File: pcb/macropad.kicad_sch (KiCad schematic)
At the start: 17 parts, among them J1 OLED_DISPLAY, SW1 SW_Push, SW2 SW_Push, SW3 SW_Push, SW4 SW_Push, SW5 RotaryEncoder_Switch, SW6 SW_Push, U1 Seeed Studio XIAO RP2040

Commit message: V1.2 - Fixed the LED symbols and retraced everything
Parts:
- D7, D8, D9: footprint Hackpad:SK6812MINI-E_fixed -> LED_SMD:LED_SK6812MINI-E_3.2x2.8mm_P1.5mm_ReverseMount; symbol LED:WS2812B -> LED:SK6812MINI-E
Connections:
- net GND: now also D7.1 (VSS), D8.1 (VSS), D9.1 (VSS); no longer D7.3 (VSS), D8.3 (VSS), D9.3 (VSS)
- net VCC: now also D7.3 (VDD), D8.3 (VDD), D9.3 (VDD); no longer D7.1 (VDD), D8.1 (VDD), D9.1 (VDD)
- net at D9.2 (DIN): now also U1.11 (PA6_A10_D10_MOSI); no longer D8.4 (DIN)
- net at D9.4 (DOUT): now also D8.2 (DIN); no longer U1.11 (PA6_A10_D10_MOSI)
- net at D7.2 (DIN): now also D8.4 (DOUT)
- net at D7.4 (DOUT): no longer D8.2 (DOUT)
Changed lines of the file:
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@@
 	)
 	(symbol
-		(lib_id "LED:WS2812B")
+		(lib_id "LED:SK6812MINI-E")
 		(at 228.6 74.93 90)
 		(unit 1)
@@
 			)
 		)
-		(property "Footprint" "Hackpad:SK6812MINI-E_fixed"
+		(property "Footprint" "LED_SMD:LED_SK6812MINI-E_3.2x2.8mm_P1.5mm_ReverseMount"
 			(at 236.22 73.66 0)
 			(hide yes)
@@
 			)
 		)
-		(property "Datasheet" "https://cdn-shop.adafruit.com/datasheets/WS2812B.pdf"
+		(property "Datasheet" "https://www.lcsc.com/datasheet/C5149201.pdf"
 			(at 238.125 72.39 0)
 			(hide yes)
@@
 	)
 	(symbol
-		(lib_id "LED:WS2812B")
+		(lib_id "LED:SK6812MINI-E")
 		(at 228.6 27.94 90)
 		(unit 1)
@@
 			)
 		)
-		(property "Footprint" "Hackpad:SK6812MINI-E_fixed"
+		(property "Footprint" "LED_SMD:LED_SK6812MINI-E_3.2x2.8mm_P1.5mm_ReverseMount"
 			(at 236.22 26.67 0)
 			(hide yes)
@@
 			)
 		)
-		(property "Datasheet" "https://cdn-shop.adafruit.com/datasheets/WS2812B.pdf"
+		(property "Datasheet" "https://www.lcsc.com/datasheet/C5149201.pdf"
 			(at 238.125 25.4 0)
 			(hide yes)
@@
 	)
 	(symbol
-		(lib_id "LED:WS2812B")
+		(lib_id "LED:SK6812MINI-E")
 		(at 228.6 52.07 90)
 		(unit 1)
@@
 			)
 		)
-		(property "Footprint" "Hackpad:SK6812MINI-E_fixed"
+		(property "Footprint" "LED_SMD:LED_SK6812MINI-E_3.2x2.8mm_P1.5mm_ReverseMount"
 			(at 236.22 50.8 0)
 			(hide yes)
@@
 			)
 		)
-		(property "Datasheet" "https://cdn-shop.adafruit.com/datasheets/WS2812B.pdf"
+		(property "Datasheet" "https://www.lcsc.com/datasheet/C5149201.pdf"
 			(at 238.125 49.53 0)
 			(hide yes)

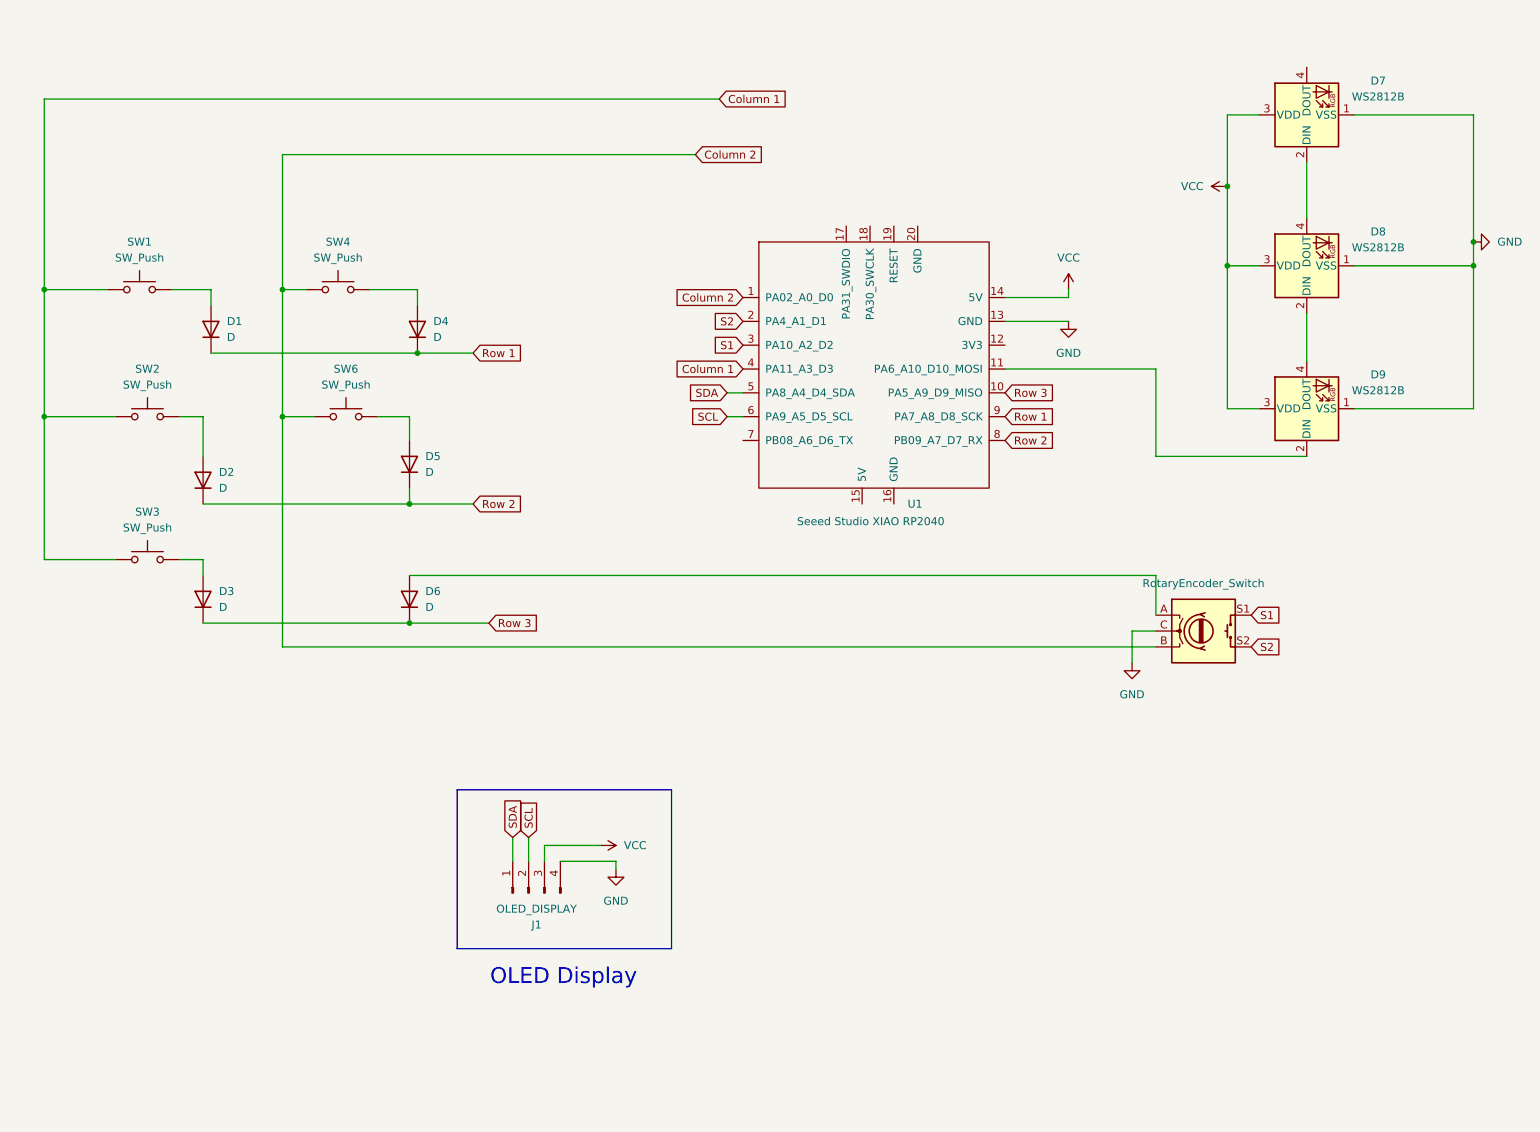
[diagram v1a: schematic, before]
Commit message: V1.3 - Added switch LEDs and GND fields
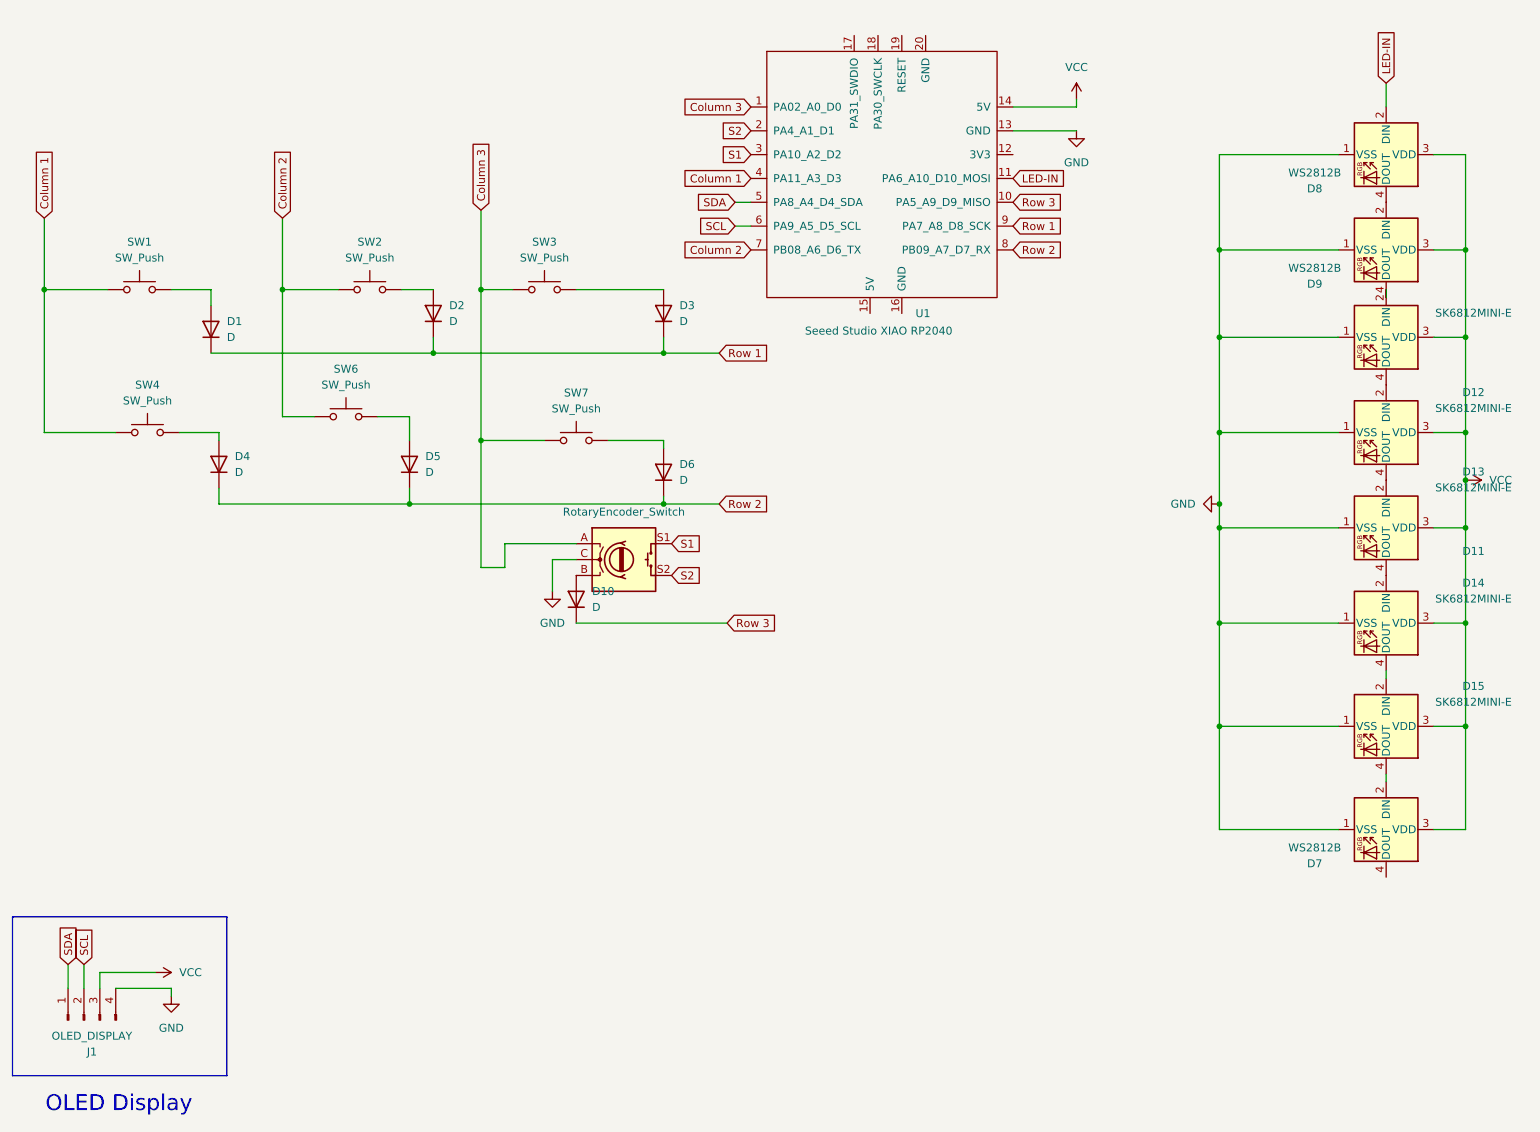
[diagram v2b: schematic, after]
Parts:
- added D10: D, Diode_THT:D_DO-35_SOD27_P7.62mm_Horizontal, symbol Device:D
- added D11, D12, D13, D14, D15: SK6812MINI-E, Cherry-MX:MX_SK6812MINI-E, symbol LED:SK6812MINI-E
- added SW7: SW_Push, Button_Switch_Keyboard:SW_Cherry_MX_1.00u_PCB, symbol Switch:SW_Push
- D9: footprint LED_SMD:LED_SK6812MINI-E_3.2x2.8mm_P1.5mm_ReverseMount -> Cherry-MX:MX_SK6812MINI-E
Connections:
- net Column 1: now also SW4.1; no longer SW2.1, SW3.1
- net Column 2: now also SW2.1, U1.7 (PB08_A6_D6_TX); no longer SW4.1, SW5.B, U1.1 (PA02_A0_D0)
- net GND: now also D11.1 (VSS), D12.1 (VSS), D13.1 (VSS), D14.1 (VSS), D15.1 (VSS)
- net Row 1: now also D2.1 (K), D3.1 (K); no longer D4.1 (K)
- net Row 2: now also D4.1 (K), D6.1 (K); no longer D2.1 (K)
- net Row 3: now also D10.1 (K); no longer D3.1 (K), D6.1 (K)
- net VCC: now also D11.3 (VDD), D12.3 (VDD), D13.3 (VDD), D14.3 (VDD), D15.3 (VDD)
- net at D9.2 (DIN): now also D8.4 (DOUT); no longer U1.11 (PA6_A10_D10_MOSI)
- net at D9.4 (DOUT): now also D11.2 (DIN); no longer D8.2 (DIN)
- net at D6.2 (A): now also SW7.2; no longer SW5.A
- net at D7.2 (DIN): now also D15.4 (DOUT); no longer D8.4 (DOUT)
- new net: D11.4 (DOUT), D12.2 (DIN)
- new net: D13.4 (DOUT), D14.2 (DIN)
- new net: D14.4 (DOUT), D15.2 (DIN)
- new net: D10.2 (A), SW5.B
- new net: D12.4 (DOUT), D13.2 (DIN)
- new net Column 3: SW3.1, SW5.A, SW7.1, U1.1 (PA02_A0_D0)
- new net LED-IN: D8.2 (DIN), U1.11 (PA6_A10_D10_MOSI)
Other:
- moved on the sheet: D2, D3, D4, D6, D7, D8, D9, J1, SW2, SW3, SW4, U1

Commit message: V1.5 - Fixed faulty encoder wiring, retraced
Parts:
- D11, D12, D13, D14, D15, D9: footprint Cherry-MX:MX_SK6812MINI-E -> Libraries:MX_SK6812MINI-E
- D7, D8: footprint LED_SMD:LED_SK6812MINI-E_3.2x2.8mm_P1.5mm_ReverseMount -> Libraries:SK6812MINI-E_fixed
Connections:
- net Column 3: now also SW5.S1; no longer SW5.A
- net at D10.2 (A): now also SW5.S2; no longer SW5.B
- net S1 renamed EN_B
- net EN_B: now also SW5.B; no longer SW5.S1
- net S2 renamed EN_A
- net EN_A: now also SW5.A; no longer SW5.S2
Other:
- moved on the sheet: D10
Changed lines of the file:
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@@
 	(wire
 		(pts
+			(xy 100.33 92.71) (xy 132.08 92.71)
+		)
+		(stroke
+			(width 0)
+			(type default)
+		)
+	)
+	(wire
+		(pts
 			(xy 233.68 125.73) (xy 214.63 125.73)
 		)
@@
 	(wire
 		(pts
+			(xy 111.76 105.41) (xy 127 105.41)
+		)
+		(stroke
+			(width 0)
+			(type default)
+		)
+	)
+	(wire
+		(pts
 			(xy 125.73 80.01) (xy 125.73 81.28)
 		)
@@
 	(wire
 		(pts
+			(xy 132.08 92.71) (xy 132.08 96.52)
+		)
+		(stroke
+			(width 0)
+			(type default)
+		)
+	)
+	(wire
+		(pts
 			(xy 33.02 163.83) (xy 33.02 167.64)
 		)
@@
 	(wire
 		(pts
-			(xy 214.63 109.22) (xy 214.63 93.98)
+			(xy 113.03 130.81) (xy 113.03 115.57)
 		)
 		(stroke
@@
 	(wire
 		(pts
-			(xy 88.9 66.04) (xy 125.73 66.04)
+			(xy 214.63 109.22) (xy 214.63 93.98)
 		)
 		(stroke
@@
 	(wire
 		(pts
-			(xy 100.33 100.33) (xy 100.33 96.52)
+			(xy 88.9 66.04) (xy 125.73 66.04)
 		)
 		(stroke
@@
 	(wire
 		(pts
+			(xy 113.03 115.57) (xy 135.89 115.57)
+		)
+		(stroke
+			(width 0)
+			(type default)
+		)
+	)
+	(wire
+		(pts
 			(xy 30.48 163.83) (xy 30.48 167.64)
 		)
@@
 	(wire
 		(pts
+			(xy 111.76 123.19) (xy 111.76 105.41)
+		)
+		(stroke
+			(width 0)
+			(type default)
+		)
+	)
+	(wire
+		(pts
 			(xy 214.63 109.22) (xy 233.68 109.22)
 		)
@@
 	(wire
 		(pts
-			(xy 111.76 109.22) (xy 135.89 109.22)
+			(xy 111.76 130.81) (xy 113.03 130.81)
 		)
 		(stroke
@@
 	(wire
 		(pts
+			(xy 127 105.41) (xy 127 101.6)
+		)
+		(stroke
+			(width 0)
+			(type default)
+		)
+	)
+	(wire
+		(pts
 			(xy 96.52 55.88) (xy 96.52 80.01)
 		)
@@
 	(wire
 		(pts
+			(xy 100.33 92.71) (xy 100.33 100.33)
+		)
+		(stroke
+			(width 0)
+			(type default)
+		)
+	)
+	(wire
+		(pts
 			(xy 214.63 49.53) (xy 233.68 49.53)
 		)
@@
 	(wire
 		(pts
-			(xy 241.3 118.11) (xy 241.3 116.84)
+			(xy 132.08 96.52) (xy 127 96.52)
 		)
 		(stroke
@@
 	(wire
 		(pts
-			(xy 191.77 26.67) (xy 191.77 25.4)
+			(xy 241.3 118.11) (xy 241.3 116.84)
 		)
 		(stroke
@@
 	(wire
 		(pts
-			(xy 254 109.22) (xy 254 93.98)
+			(xy 191.77 26.67) (xy 191.77 25.4)
 		)
 		(stroke
@@
 	(wire
 		(pts
-			(xy 100.33 96.52) (xy 111.76 96.52)
+			(xy 254 109.22) (xy 254 93.98)
 		)
 		(stroke
@@
 	(global_label "Row 3"
 		(shape input)
-		(at 135.89 109.22 0)
+		(at 135.89 115.57 0)
 		(fields_autoplaced yes)
 		(effects
@@
 		)
 		(property "Intersheetrefs" "${INTERSHEET_REFS}"
-			(at 144.8018 109.22 0)
+			(at 144.8018 115.57 0)
 			(hide yes)
 			(show_name no)
@@
 		)
 	)
-	(global_label "S1"
+	(global_label "EN_B"
 		(shape input)
 		(at 139.7 34.29 180)
@@
 		)
 		(property "Intersheetrefs" "${INTERSHEET_REFS}"
-			(at 134.2958 34.29 0)
+			(at 131.9977 34.29 0)
 			(hide yes)
 			(show_name no)
@@
 		)
 	)
-	(global_label "S1"
+	(global_label "EN_A"
 		(shape input)
-		(at 127 96.52 0)
+		(at 111.76 96.52 180)
 		(fields_autoplaced yes)
 		(effects
@@
 				(size 1.27 1.27)
 			)
-			(justify left)
+			(justify right)
 		)
 		(property "Intersheetrefs" "${INTERSHEET_REFS}"
-			(at 132.4042 96.52 0)
+			(at 104.2391 96.52 0)
 			(hide yes)
 			(show_name no)
@@
 					(size 1.27 1.27)
 				)
-				(justify left)
+				(justify right)
 			)
 		)
@@
 		)
 	)
-	(global_label "S2"
+	(global_label "EN_B"
 		(shape input)
-		(at 127 101.6 0)
+		(at 111.76 101.6 180)
 		(fields_autoplaced yes)
 		(effects
@@
 				(size 1.27 1.27)
 			)
-			(justify left)
+			(justify right)
 		)
 		(property "Intersheetrefs" "${INTERSHEET_REFS}"
-			(at 132.4042 101.6 0)
+			(at 104.0577 101.6 0)
 			(hide yes)
 			(show_name no)
@@
 					(size 1.27 1.27)
 				)
-				(justify left)
+				(justify right)
 			)
 		)
@@
 		)
 	)
-	(global_label "S2"
+	(global_label "EN_A"
 		(shape input)
 		(at 139.7 30.48 180)
@@
 		)
 		(property "Intersheetrefs" "${INTERSHEET_REFS}"
-			(at 134.2958 30.48 0)
+			(at 132.1791 30.48 0)
 			(hide yes)
 			(show_name no)
@@
 			)
 		)
-		(property "Footprint" "Cherry-MX:MX_SK6812MINI-E"
+		(property "Footprint" "Libraries:MX_SK6812MINI-E"
 			(at 233.68 64.77 0)
 			(hide yes)
@@
 			)
 		)
-		(property "Footprint" "Cherry-MX:MX_SK6812MINI-E"
+		(property "Footprint" "Libraries:MX_SK6812MINI-E"
 			(at 233.68 50.8 0)
 			(hide yes)
@@
 			)
 		)
-		(property "Footprint" "Cherry-MX:MX_SK6812MINI-E"
+		(property "Footprint" "Libraries:MX_SK6812MINI-E"
 			(at 233.68 110.49 0)
 			(hide yes)
@@
 	(symbol
 		(lib_id "Device:D")
-		(at 111.76 105.41 90)
+		(at 111.76 127 90)
 		(unit 1)
 		(body_style 1)
@@
 		(fields_autoplaced yes)
 		(property "Reference" "D10"
-			(at 114.3 104.1399 90)
+			(at 114.3 125.7299 90)
 			(show_name no)
 			(do_not_autoplace no)
@@
 		)
 		(property "Value" "D"
-			(at 114.3 106.6799 90)
+			(at 114.3 128.2699 90)
 			(show_name no)
 			(do_not_autoplace no)
@@
 		)
 		(property "Footprint" "Diode_THT:D_DO-35_SOD27_P7.62mm_Horizontal"
-			(at 111.76 105.41 0)
+			(at 111.76 127 0)
 			(hide yes)
 			(show_name no)
@@
 		)
 		(property "Datasheet" ""
-			(at 111.76 105.41 0)
+			(at 111.76 127 0)
 			(hide yes)
 			(show_name no)
@@
 		)
 		(property "Description" "Diode"
-			(at 111.76 105.41 0)
+			(at 111.76 127 0)
 			(hide yes)
 			(show_name no)
@@
 		)
 		(property "Sim.Device" "D"
-			(at 111.76 105.41 0)
+			(at 111.76 127 0)
 			(hide yes)
 			(show_name no)
@@
 		)
 		(property "Sim.Pins" "1=K 2=A"
-			(at 111.76 105.41 0)
+			(at 111.76 127 0)
 			(hide yes)
 			(show_name no)
@@
 			)
 		)
-		(property "Footprint" "Cherry-MX:MX_SK6812MINI-E"
+		(property "Footprint" "Libraries:MX_SK6812MINI-E"
 			(at 233.68 95.25 0)
 			(hide yes)
@@
 			)
 		)
-		(property "Footprint" "Cherry-MX:MX_SK6812MINI-E"
+		(property "Footprint" "Libraries:MX_SK6812MINI-E"
 			(at 233.68 80.01 0)
 			(hide yes)
@@
 			)
 		)
-		(property "Footprint" "LED_SMD:LED_SK6812MINI-E_3.2x2.8mm_P1.5mm_ReverseMount"
+		(property "Footprint" "Libraries:SK6812MINI-E_fixed"
 			(at 233.68 143.51 0)
 			(hide yes)
@@
 			)
 		)
-		(property "Footprint" "LED_SMD:LED_SK6812MINI-E_3.2x2.8mm_P1.5mm_ReverseMount"
+		(property "Footprint" "Libraries:SK6812MINI-E_fixed"
 			(at 233.68 35.56 0)
 			(hide yes)
@@
 			)
 		)
-		(property "Footprint" "Cherry-MX:MX_SK6812MINI-E"
+		(property "Footprint" "Libraries:MX_SK6812MINI-E"
 			(at 233.68 127 0)
 			(hide yes)
